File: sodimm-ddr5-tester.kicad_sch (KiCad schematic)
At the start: 2 parts, among them M1001 Mech_Lightpipe_Mentor_1296.20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

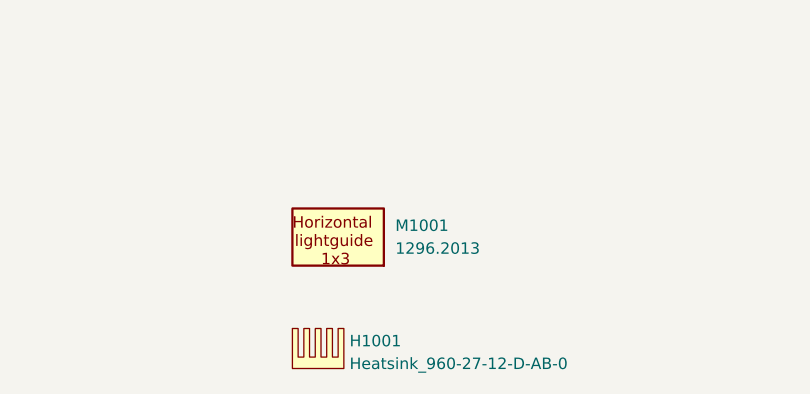
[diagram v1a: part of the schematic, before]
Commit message: Re-annotate schematic
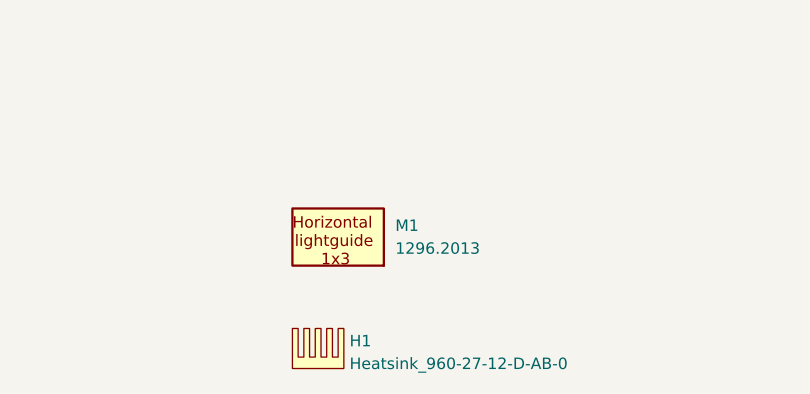
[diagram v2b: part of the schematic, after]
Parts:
- renumbered H1001 to H1, M1001 to M1

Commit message: Add local libraries
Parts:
- H1: footprint antmicro-footprints:Heatsink_960-27-12-D-AB-0 -> sodimm-ddr5-tester-footprints:Heatsink_960-27-12-D-AB-0; symbol antmicroMechanicalParts:Heatsink_960-27-12-D-AB-0 -> sodimm-ddr5-tester:Heatsink_960-27-12-D-AB-0

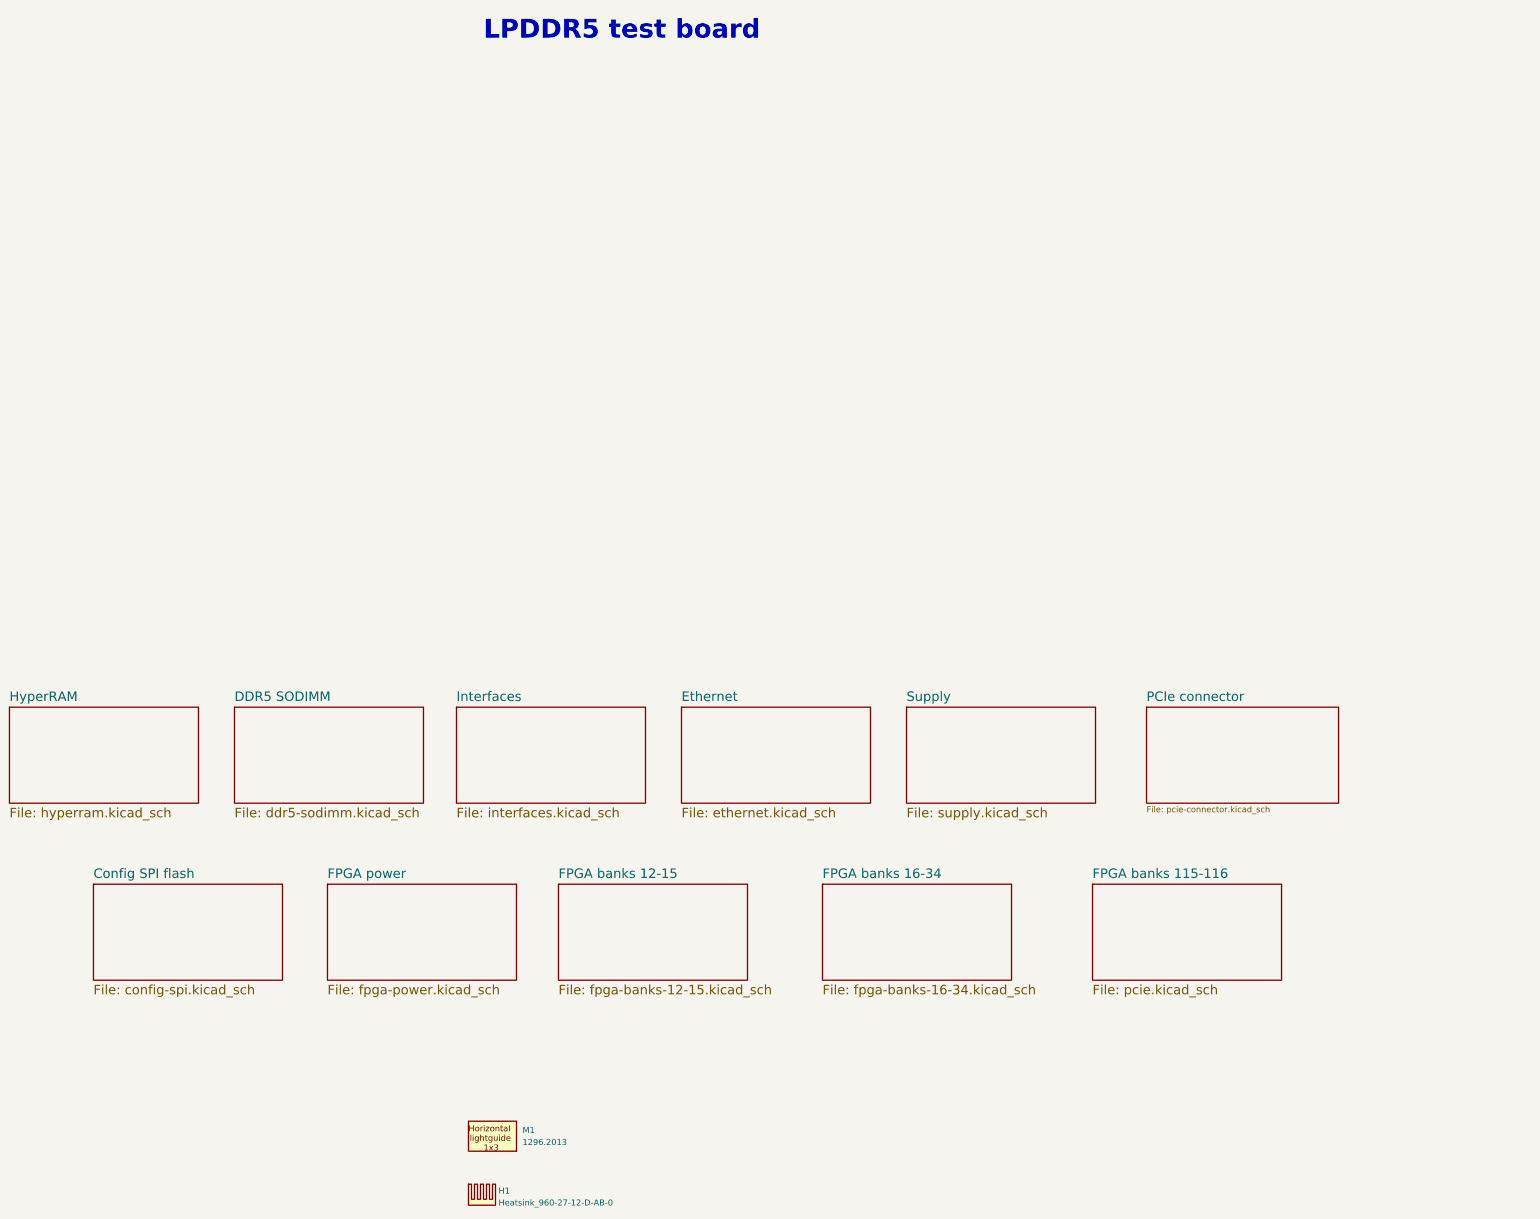
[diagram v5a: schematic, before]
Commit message: Define DDR5, HyperBus and I2C buses. Connect HyperRAM with hierarchical bus
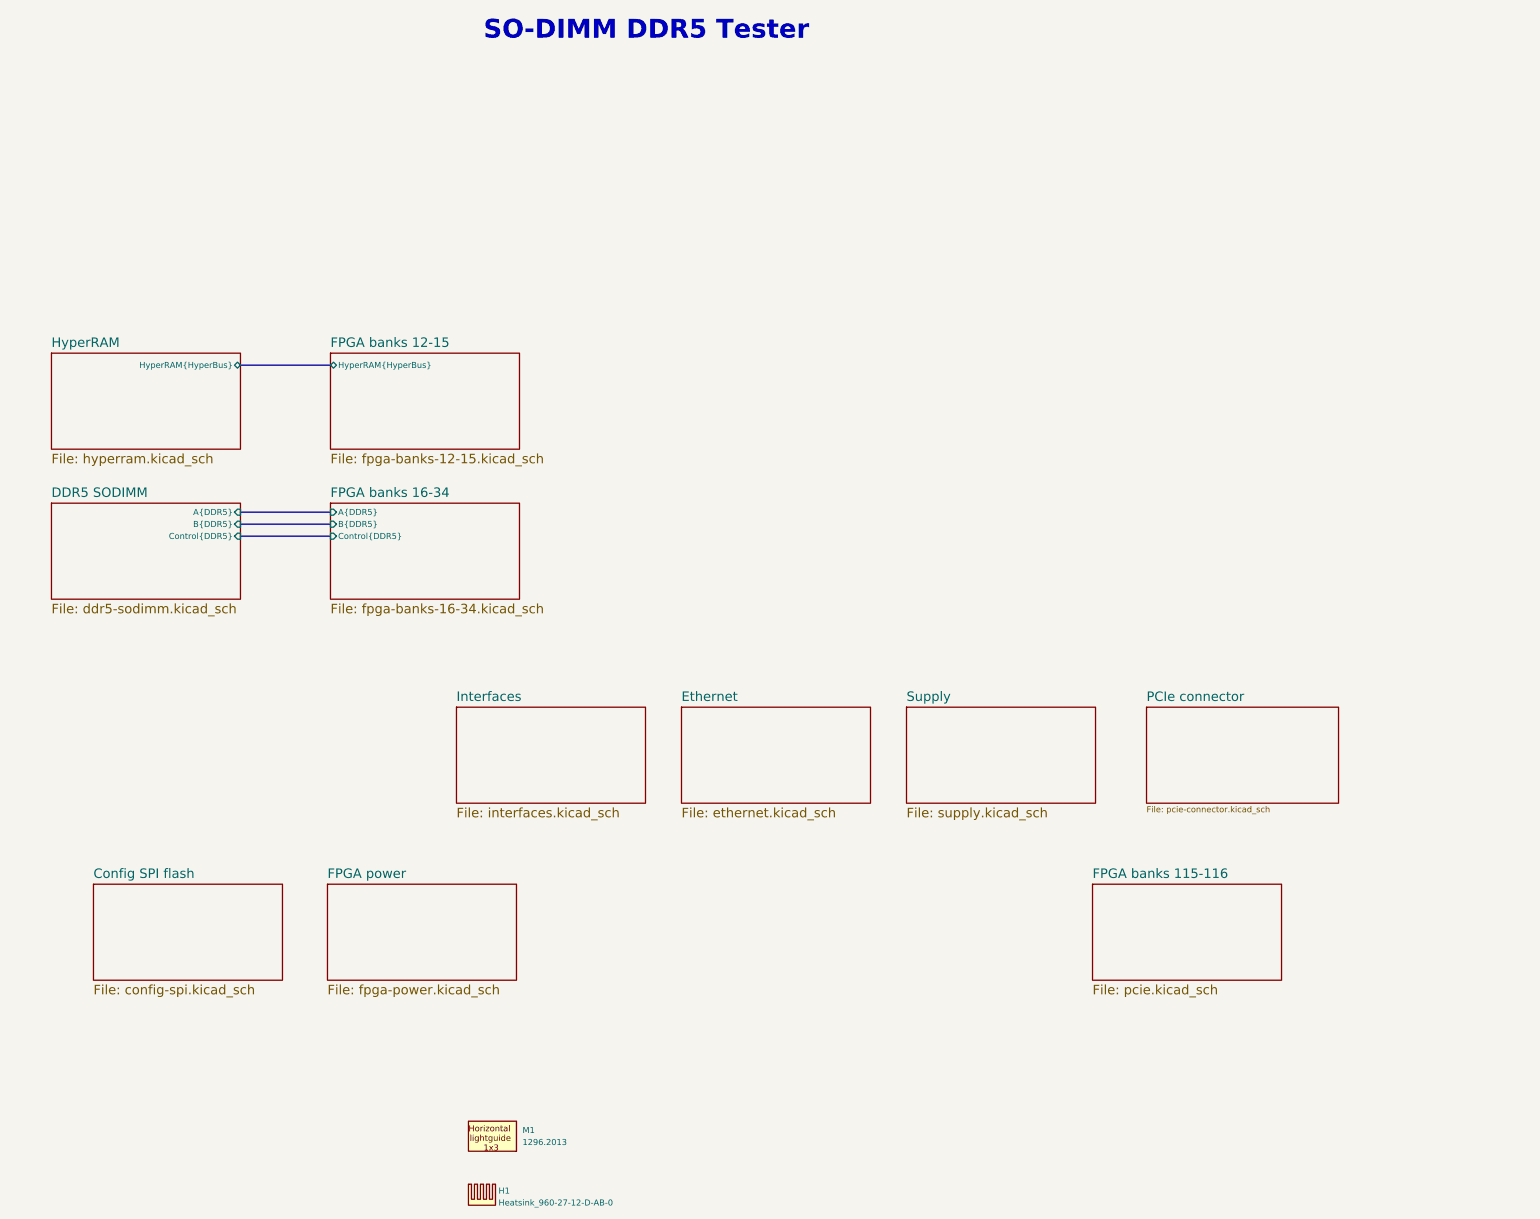
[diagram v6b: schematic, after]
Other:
- sheet DDR5 SODIMM ports: added A{DDR5}, B{DDR5}, Control{DDR5}; removed none
- sheet FPGA banks 12-15 ports: added HyperRAM{HyperBus}; removed none
- sheet FPGA banks 16-34 ports: added A{DDR5}, B{DDR5}, Control{DDR5}; removed none
- sheet HyperRAM ports: added HyperRAM{HyperBus}; removed none
- note added: "SO-DIMM DDR5 Tester"
- note removed: "LPDDR5 test board"
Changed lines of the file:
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@@
     (comment 2 "Antmicro Ltd")
+  )
+  (bus_alias "I^{2}C" (members "SDA" "SCL"))
+  (bus_alias "DDR5" (members "DQ[0..31]" "CA[0..12]" "DM[0..3]" "CB[0..3]" "DQS0_P" "DQS0_N" "DQS1_P" "DQS1_N" "DQS2_P" "DQS2_N" "DQS3_P" "DQS3_N" "DQS4_P" "DQS4_N" "CK0_P" "CK0_N" "CK1_P" "CK1_N" "~{CS0}" "~{CS1}" "~{ALERT}"))
+  (bus_alias "HyperBus" (members "~{CS}" "CK_P" "CK_N" "RWDS" "DQ[0..7]" "~{RESET}"))
+  (bus (pts (xy 120.65 135.255) (xy 139.7 135.255))
+    (stroke (width 0) (type default) (color 0 0 0 0))
+  )
+  (bus (pts (xy 120.65 140.335) (xy 139.7 140.335))
+    (stroke (width 0) (type default) (color 0 0 0 0))
+  )
+  (bus (pts (xy 120.65 104.14) (xy 139.7 104.14))
+    (stroke (width 0) (type default) (color 0 0 0 0))
+  )
+  (bus (pts (xy 120.65 137.795) (xy 139.7 137.795))
+    (stroke (width 0) (type default) (color 0 0 0 0))
   )
   (image (at 38.1 271.6022) (scale 0.4)
@@
     )
   )
-  (text "LPDDR5 test board" (at 172.085 35.56 0)
+  (text "SO-DIMM DDR5 Tester" (at 172.085 35.56 0)
     (effects (font (size 3.9878 3.9878) (thickness 0.7976) bold) (justify left bottom))
   )
@@
     )
   )
-  (sheet (at 71.755 176.53) (size 40.005 20.32) (fields_autoplaced)
+  (sheet (at 80.645 101.6) (size 40.005 20.32) (fields_autoplaced)
     (stroke (width 0) (type solid) (color 0 0 0 0))
     (fill (color 0 0 0 0.0000))
-    (property "Sheet name" "HyperRAM" (id 0) (at 71.755 175.4501 0)
+    (property "Sheet name" "HyperRAM" (id 0) (at 80.645 100.5201 0)
       (effects (font (size 2.0066 2.0066)) (justify left bottom))
     )
-    (property "Sheet file" "hyperram.kicad_sch" (id 1) (at 71.755 197.7292 0)
+    (property "Sheet file" "hyperram.kicad_sch" (id 1) (at 80.645 122.7992 0)
       (effects (font (size 2.0066 2.0066)) (justify left top))
+    )
+    (pin "HyperRAM{HyperBus}" bidirectional (at 120.65 104.14 0)
+      (effects (font (size 1.27 1.27)) (justify right))
     )
   )
@@
     )
   )
-  (sheet (at 119.38 176.53) (size 40.005 20.32) (fields_autoplaced)
+  (sheet (at 80.645 133.35) (size 40.005 20.32) (fields_autoplaced)
     (stroke (width 0) (type solid) (color 0 0 0 0))
     (fill (color 0 0 0 0.0000))
-    (property "Sheet name" "DDR5 SODIMM" (id 0) (at 119.38 175.4501 0)
+    (property "Sheet name" "DDR5 SODIMM" (id 0) (at 80.645 132.2701 0)
       (effects (font (size 2.0066 2.0066)) (justify left bottom))
     )
-    (property "Sheet file" "ddr5-sodimm.kicad_sch" (id 1) (at 119.38 197.7292 0)
+    (property "Sheet file" "ddr5-sodimm.kicad_sch" (id 1) (at 80.645 154.5492 0)
       (effects (font (size 2.0066 2.0066)) (justify left top))
     )
+    (pin "B{DDR5}" input (at 120.65 137.795 0)
+      (effects (font (size 1.27 1.27)) (justify right))
+    )
+    (pin "A{DDR5}" input (at 120.65 135.255 0)
+      (effects (font (size 1.27 1.27)) (justify right))
+    )
+    (pin "Control{DDR5}" input (at 120.65 140.335 0)
+      (effects (font (size 1.27 1.27)) (justify right))
+    )
   )
-  (sheet (at 187.96 213.995) (size 40.005 20.32) (fields_autoplaced)
+  (sheet (at 139.7 101.6) (size 40.005 20.32) (fields_autoplaced)
     (stroke (width 0) (type solid) (color 0 0 0 0))
     (fill (color 0 0 0 0.0000))
-    (property "Sheet name" "FPGA banks 12-15" (id 0) (at 187.96 212.9151 0)
+    (property "Sheet name" "FPGA banks 12-15" (id 0) (at 139.7 100.5201 0)
       (effects (font (size 2.0066 2.0066)) (justify left bottom))
     )
-    (property "Sheet file" "fpga-banks-12-15.kicad_sch" (id 1) (at 187.96 235.1942 0)
+    (property "Sheet file" "fpga-banks-12-15.kicad_sch" (id 1) (at 139.7 122.7992 0)
       (effects (font (size 2.0066 2.0066)) (justify left top))
     )
+    (pin "HyperRAM{HyperBus}" bidirectional (at 139.7 104.14 180)
+      (effects (font (size 1.27 1.27)) (justify left))
+    )
   )
-  (sheet (at 243.84 213.995) (size 40.005 20.32) (fields_autoplaced)
+  (sheet (at 139.7 133.35) (size 40.005 20.32) (fields_autoplaced)
     (stroke (width 0) (type solid) (color 0 0 0 0))
     (fill (color 0 0 0 0.0000))
-    (property "Sheet name" "FPGA banks 16-34" (id 0) (at 243.84 212.9151 0)
+    (property "Sheet name" "FPGA banks 16-34" (id 0) (at 139.7 132.2701 0)
       (effects (font (size 2.0066 2.0066)) (justify left bottom))
     )
-    (property "Sheet file" "fpga-banks-16-34.kicad_sch" (id 1) (at 243.84 235.1942 0)
+    (property "Sheet file" "fpga-banks-16-34.kicad_sch" (id 1) (at 139.7 154.5492 0)
       (effects (font (size 2.0066 2.0066)) (justify left top))
     )
+    (pin "A{DDR5}" input (at 139.7 135.255 180)
+      (effects (font (size 1.27 1.27)) (justify left))
+    )
+    (pin "B{DDR5}" input (at 139.7 137.795 180)
+      (effects (font (size 1.27 1.27)) (justify left))
+    )
+    (pin "Control{DDR5}" input (at 139.7 140.335 180)
+      (effects (font (size 1.27 1.27)) (justify left))
+    )
   )

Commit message: Connect DDR hierarchical labels. Define and connect JTAG, RGMII, TDMS, UART, and SDIO buses. Reorganize schematic blocks between sheets
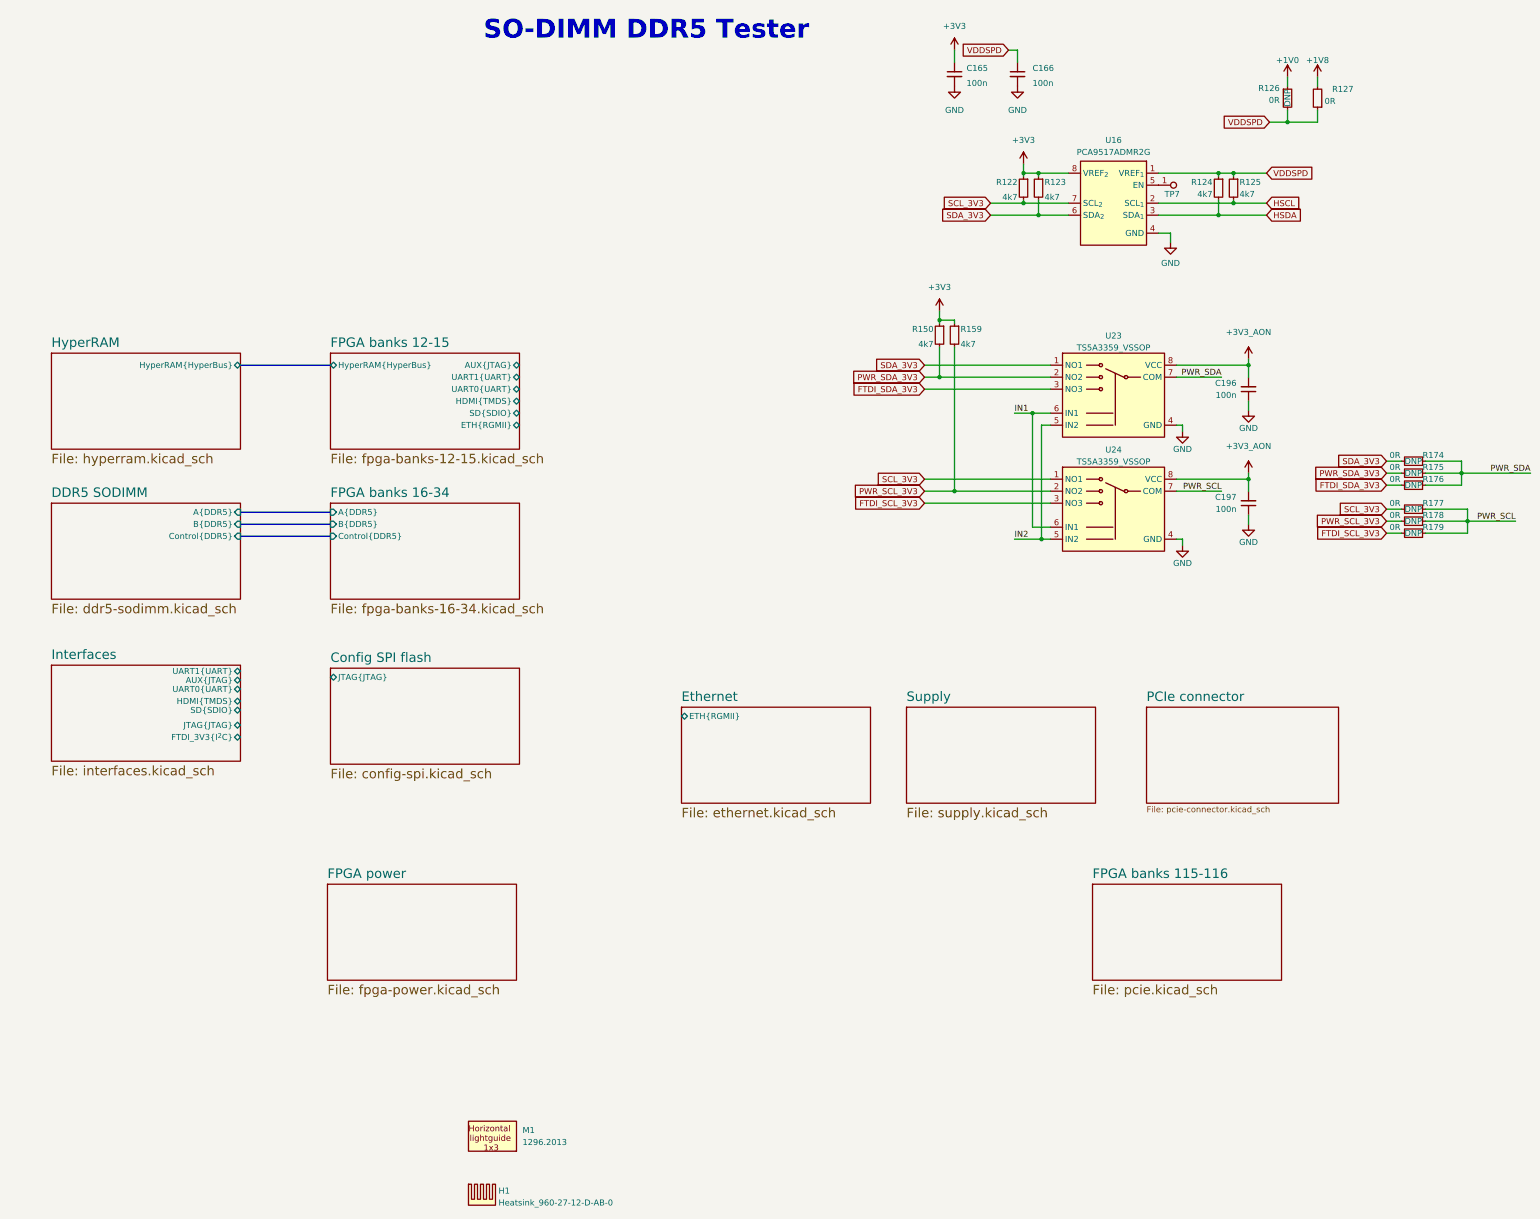
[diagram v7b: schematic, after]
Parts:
- added C165, C166, C196, C197: C_100n_0402, sodimm-ddr5-tester-footprints:C_0402_1005Metric, symbol sodimm-ddr5-tester:C_100n_0402
- added R122, R123, R124, R125, R150, R159: R_4k7_0402, sodimm-ddr5-tester-footprints:R_0402_1005Metric, symbol sodimm-ddr5-tester:R_4k7_0402
- added R126, R127, R174, R175, R176, R177, R178, R179: R_0R_0402, sodimm-ddr5-tester-footprints:R_0402_1005Metric, symbol sodimm-ddr5-tester:R_0R_0402
- added TP7: TP_1mm_SMD, sodimm-ddr5-tester-footprints:TP_SMD_1mm, symbol sodimm-ddr5-tester:TP_1mm_SMD
- added U16: PCA9517A_TSSOP, sodimm-ddr5-tester-footprints:TSSOP-8_3x3mm_P0.65mm, symbol sodimm-ddr5-tester:PCA9517A_TSSOP
- added U23, U24: TS5A3359_VSSOP, sodimm-ddr5-tester-footprints:VSSOP-8_2.3x2mm_P0.5mm, symbol sodimm-ddr5-tester:TS5A3359_VSSOP
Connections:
- new net: TP7.1, U16.5 (EN)
- new net +1V0: R126.1
- new net +1V8: R127.2
- new net +3V3: C165.1, R122.1, R123.1, R150.1, R159.1, U16.8 (VREF_{2})
- new net +3V3_AON: C196.2, C197.2, U23.8 (VCC), U24.8 (VCC)
- new net FTDI_SCL_3V3: R179.2, U24.3 (NO3)
- new net FTDI_SDA_3V3: R176.2, U23.3 (NO3)
- new net GND: C165.2, C166.2, C196.1, C197.1, U16.4 (GND), U23.4 (GND), U24.4 (GND)
- new net HSCL: R125.2, U16.2 (SCL_{1})
- new net HSDA: R124.2, U16.3 (SDA_{1})
- new net IN1: U23.6 (IN1), U24.6 (IN1)
- new net IN2: U23.5 (IN2), U24.5 (IN2)
- new net PWR_SCL: R177.1, R178.1, R179.1, U24.7 (COM)
- new net PWR_SCL_3V3: R159.2, R178.2, U24.2 (NO2)
- new net PWR_SDA: R174.1, R175.1, R176.1, U23.7 (COM)
- new net PWR_SDA_3V3: R150.2, R175.2, U23.2 (NO2)
- new net SCL_3V3: R122.2, R177.2, U16.7 (SCL_{2}), U24.1 (NO1)
- new net SDA_3V3: R123.2, R174.2, U16.6 (SDA_{2}), U23.1 (NO1)
- new net VDDSPD: C166.1, R124.1, R125.1, R126.2, R127.1, U16.1 (VREF_{1})
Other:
- sheet Config SPI flash ports: added JTAG{JTAG}; removed none
- sheet Ethernet ports: added ETH{RGMII}; removed none
- sheet FPGA banks 12-15 ports: added AUX{JTAG}, ETH{RGMII}, HDMI{TMDS}, SD{SDIO}, UART0{UART}, UART1{UART}; removed none
- sheet Interfaces ports: added AUX{JTAG}, FTDI_3V3{I^{2}C}, HDMI{TMDS}, JTAG{JTAG}, SD{SDIO}, UART0{UART}, UART1{UART}; removed none
